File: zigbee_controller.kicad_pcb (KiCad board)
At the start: 2 copper layers, 55.5 x 65 mm, 79 parts, among them J1 KF635, J10 TerminalBlock_KF301-5.0, J11 TerminalBlock_KF301-5.0, J12 TerminalBlock_KF301-5.0, J13 TerminalBlock_KF301-5.0, J3 Conn_01x06, J4 Conn_01x07, J5 Conn_01x05, P1 USB_C_Receptacle_GCT_USB4105, Q2 IRLB3813, Q3 IRLB3813, Q4 IRLB3813, Q5 IRLB3813, SW2 EN, SW4 Boot, U1 TPS54560, U2 ESP32-C6-MINI-1, U4 TC4427, U5 TC4427, U6 RT9080, U9 CH224K

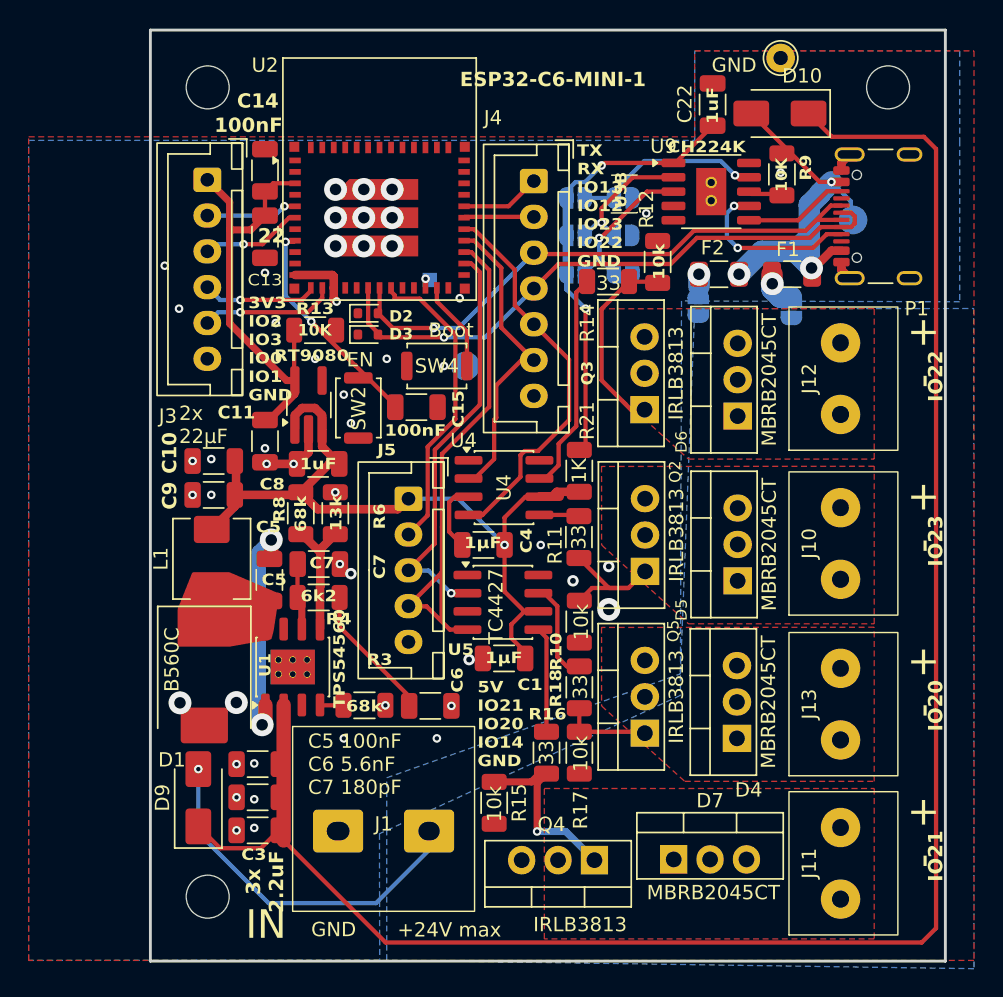
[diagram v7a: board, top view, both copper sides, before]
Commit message: Decrease board size to 55mm
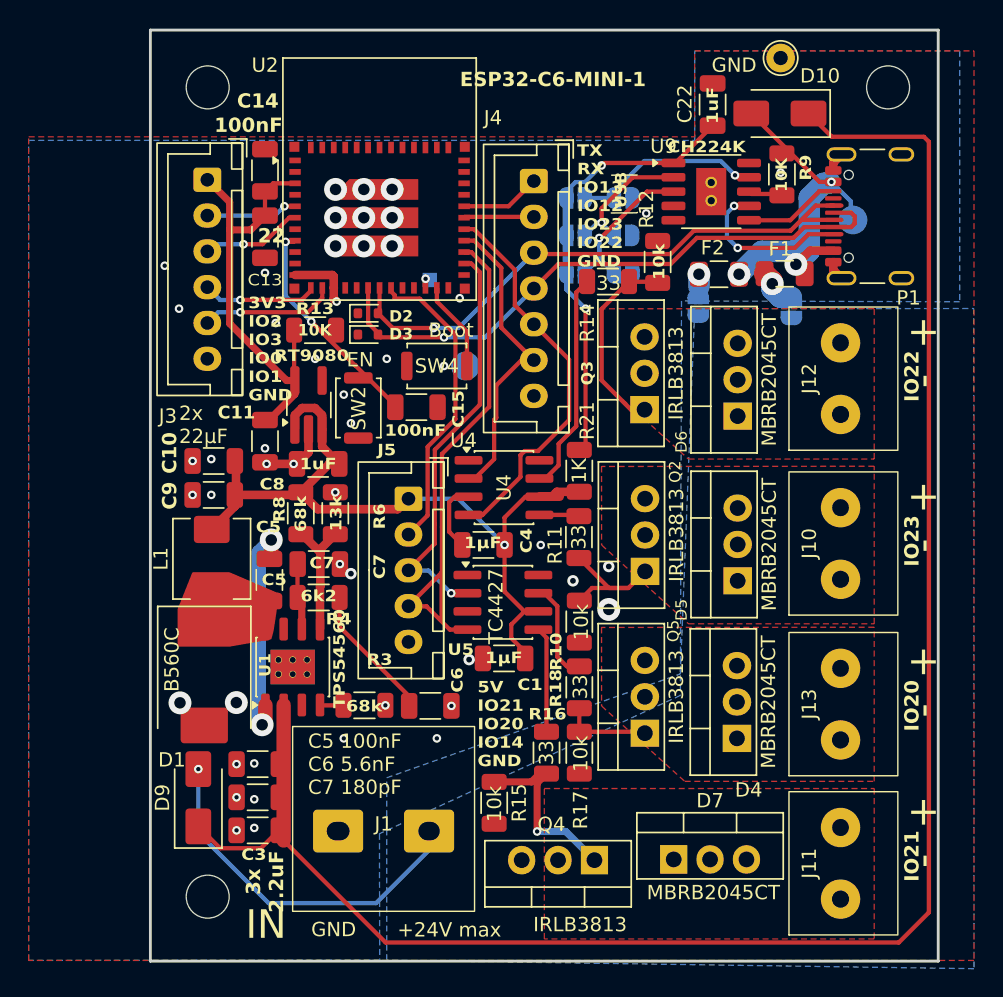
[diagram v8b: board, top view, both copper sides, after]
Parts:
- moved P1 0.57 mm to (203.9, 81.5)
- moved F1 0.52 mm to (196.8, 85.5)
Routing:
- net VBUS: track 30.3 -> 27.5 mm
- net Net-(D10-K): track 129.4 -> 128.0 mm
- net /IO13-usb: track 39.7 -> 41.0 mm
- net /CC2: track 7.29 -> 6.30 mm
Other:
- board size 55.5 x 65 mm -> 55 x 65 mm
